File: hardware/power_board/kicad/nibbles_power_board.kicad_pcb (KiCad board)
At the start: 2 copper layers, 100 x 70 mm, 65 parts, among them J10 XT30 (charger port: input), J11 XT30 (charger port: battery), J12 JST-GH 6 (charger port: I2C), J2 XT30PW-M (dock power, from th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, J3 XT30 (pack, from 4S BMS), J5 XT30 (to the 5 V lighting con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, J6 To the base board (JST-GH 8), J7 S3B-PH-K-S (dock data, from t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, J8 S2B-PH-K-S (dock LED, panel), J9 JST-GH 6 (keypad port: I2C), Q5 30V N-FET >= 15 A, Q6 30V N-FET >= 15 A, Q7 2N7002, Q8 2N7002, Q9 30V N-FET >= 15 A, U3 LM74700-Q1 (dock), U4 LM74700-Q1 (pack), U5 TPS259827ONRGET, U6 INA226AIDGSR, U7 TPS62933DRLR, U8 TCA9534PWR, U9 LM74700-Q1 (LEMO)

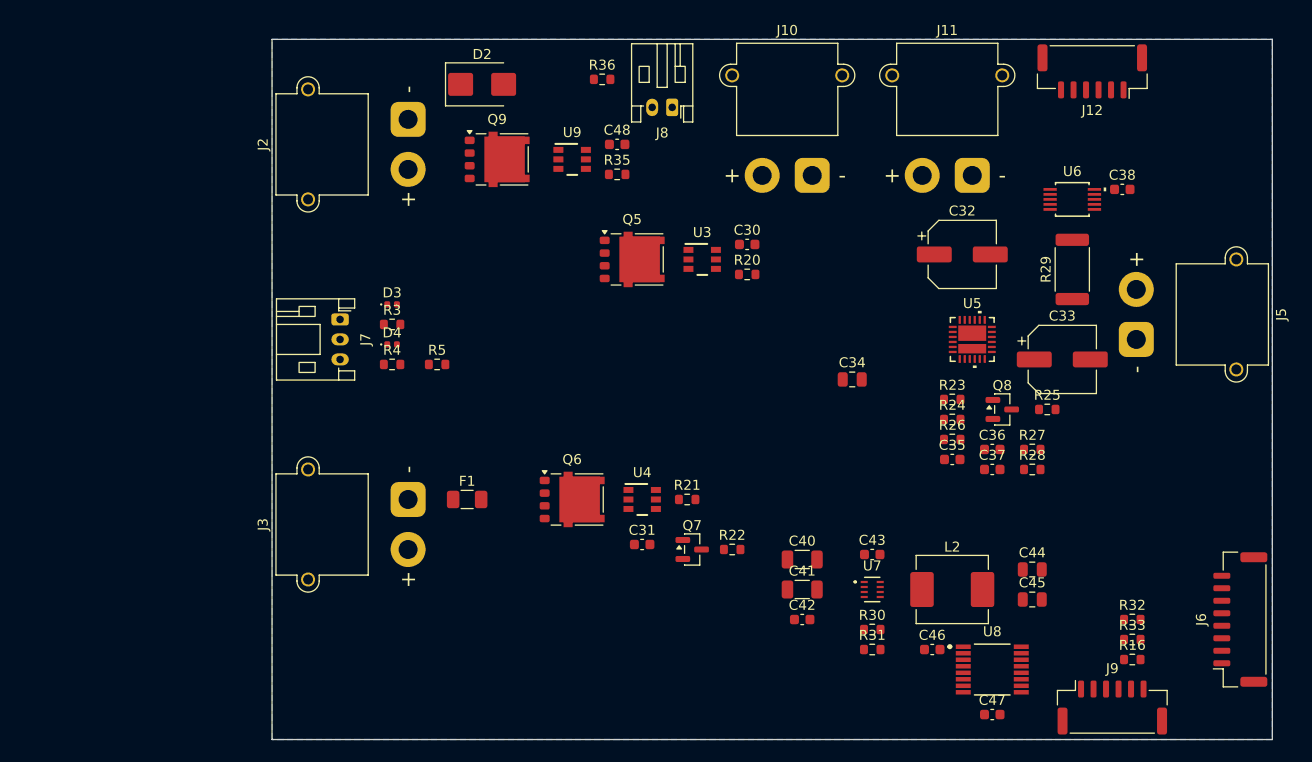
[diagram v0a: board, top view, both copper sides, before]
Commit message: Power board: one-sheet schematic drawn as wired blocks, net classes, layout in progress
- KiCad schematic merged into one page; the ideal diodes (U9/Q9, U3/Q5,
  U4/Q6), the eFuse path (U5, bulk caps, shunt R29 and INA226, J3/F1, J5)
  and the 5 V buck (U7) are now wired pin to pin instead of label to
  label. Same netlist; ITIMER, ILIM, IMON and RETRY_DLY now use KiCad's
  automatic net names (renamed to match in the board).
- The KiCad files are now the master copy for the power board; the
  generator refuses a board with tracks.
- Net classes for both boards (Power 5 mm / 3 mm, Supply 1 mm) and
  pre-defined track and via sizes in the generator.
- Placement, routing and pours on the power board so far.

Co-Authored-By: Claude Opus 5.5 <noreply@anthropic.com>
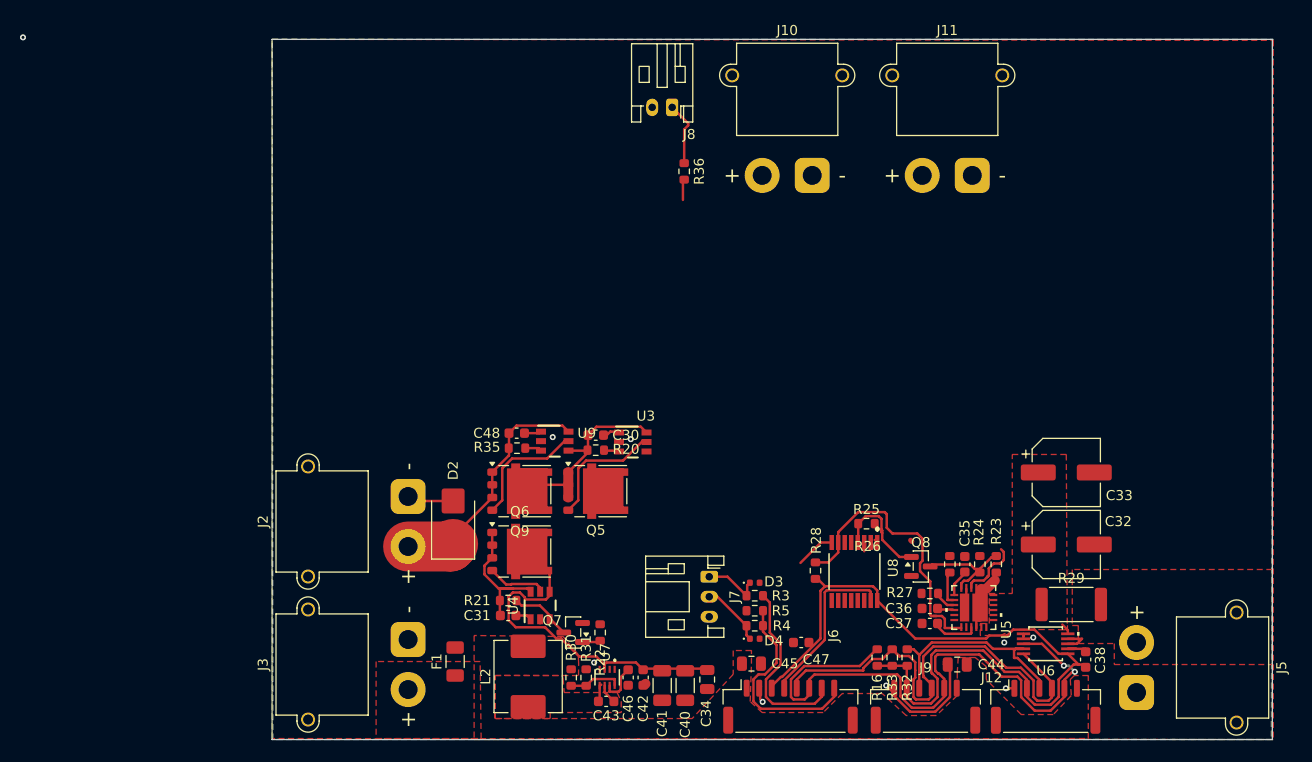
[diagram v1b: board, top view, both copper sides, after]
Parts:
- moved J12 63.7 mm to (127.3, 116.7), turned to 0 degrees
- moved C38 47.1 mm to (131.3, 112.0), turned to 90 degrees
- moved D4 46.7 mm to (98.3, 109.9)
- moved J6 45.8 mm to (101.8, 116.7), turned to 0 degrees
- moved D3 45.7 mm to (98.3, 104.3)
- moved R3 45.3 mm to (98.3, 105.6)
- moved J7 45.0 mm to (93.7, 103.7)
- moved R4 44.7 mm to (98.3, 108.6)
- moved U6 44.5 mm to (127.3, 110.4)
- moved D2 43.9 mm to (68.1, 98.3), turned to 90 degrees
- moved L2 43.3 mm to (75.6, 113.7), turned to 90 degrees
- moved R5 40.2 mm to (98.3, 107.1), turned to 180 degrees
- moved J2 37.7 mm to (63.6, 95.7)
- moved J5 35.3 mm to (136.4, 115.3)
- moved R29 33.5 mm to (129.9, 106.5), turned to 0 degrees
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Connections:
- net EFUSE_ILIM renamed Net-(U5-ILIM)
- net EFUSE_IMON renamed Net-(U5-IMON)
- net EFUSE_ITIMER renamed Net-(U5-ITIMER)
- net EFUSE_RETRY renamed Net-(U5-RETRY_DLY)
- U7 pad 1: (no net) -> unconnected-(U7-RT-Pad1)
- U7 pad 2: (no net) -> unconnected-(U7-EN-Pad2)
- U8 pad 10: (no net) -> unconnected-(U8-P5-Pad10)
- U8 pad 11: (no net) -> unconnected-(U8-P6-Pad11)
- U8 pad 12: (no net) -> unconnected-(U8-P7-Pad12)
- U8 pad 6: (no net) -> unconnected-(U8-P2-Pad6)
- U8 pad 9: (no net) -> unconnected-(U8-P4-Pad9)
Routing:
- net +3V3: track 0.00 -> 79.4 mm
- net PWR_INT: track 0.00 -> 62.8 mm, vias 0 -> 2
- net PWR_SCL: track 0.00 -> 47.3 mm
- net LIGHT_BUS: track 0.00 -> 43.1 mm
- net GND: track 0.00 -> 40.3 mm, vias 0 -> 8
- net PWR_SDA: track 0.00 -> 39.0 mm
- net EFUSE_PG: track 0.00 -> 28.5 mm
- net DOCK_RAW: track 0.00 -> 24.5 mm
- net DOCK_VIN: track 0.00 -> 21.9 mm
- net DOCK_DET: track 0.00 -> 20.7 mm
- net DOCK_UART: track 0.00 -> 18.4 mm
- net PACK_F: track 0.00 -> 14.2 mm
- net GATE_DOCK: track 0.00 -> 12.5 mm
- net GATE_LEMO: track 0.00 -> 12.3 mm
- net LIGHT_OFF: track 0.00 -> 10.8 mm
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- added copper zone on F.Cu, net +5V
- added copper zone on F.Cu, net BUCK_SW
- added copper zone on F.Cu, net EFUSE_OUT
- added copper zone on F.Cu, net GND
- added copper zone on F.Cu, net LIGHT_OUT
- added copper zone on F.Cu, net PACK_RAW
